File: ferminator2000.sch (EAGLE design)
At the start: 120 parts, among them CN1 MINIB, IC1 FT232RL, IC2 REF01D, Q1 STP5NA50, Q2 STP5NA50, SW1 ENCODER_SW1-PEC12, U1 DSPIC33FJ256GP510A, U2 AD8495

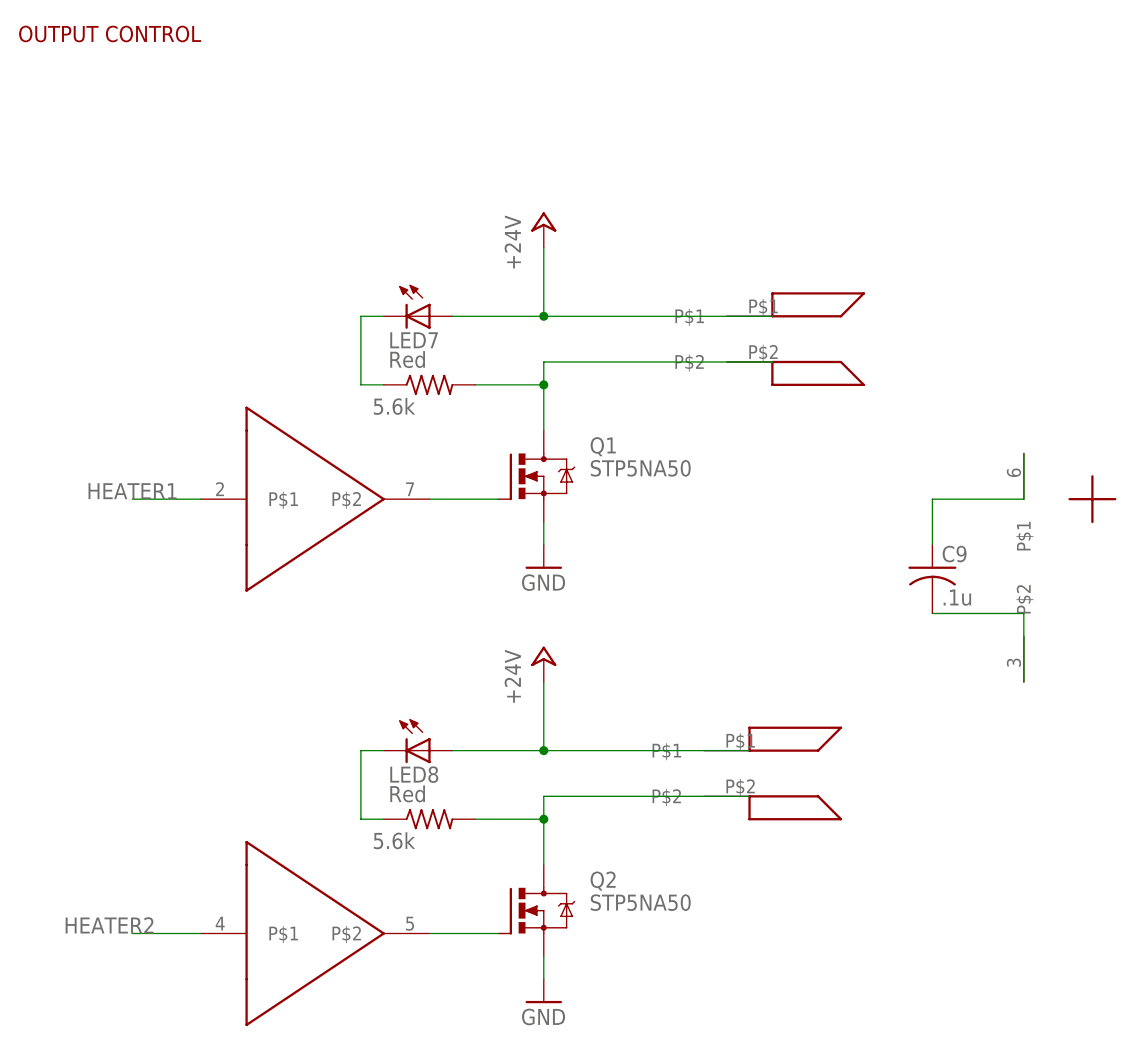
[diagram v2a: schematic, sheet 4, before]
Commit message: added power to TC4427
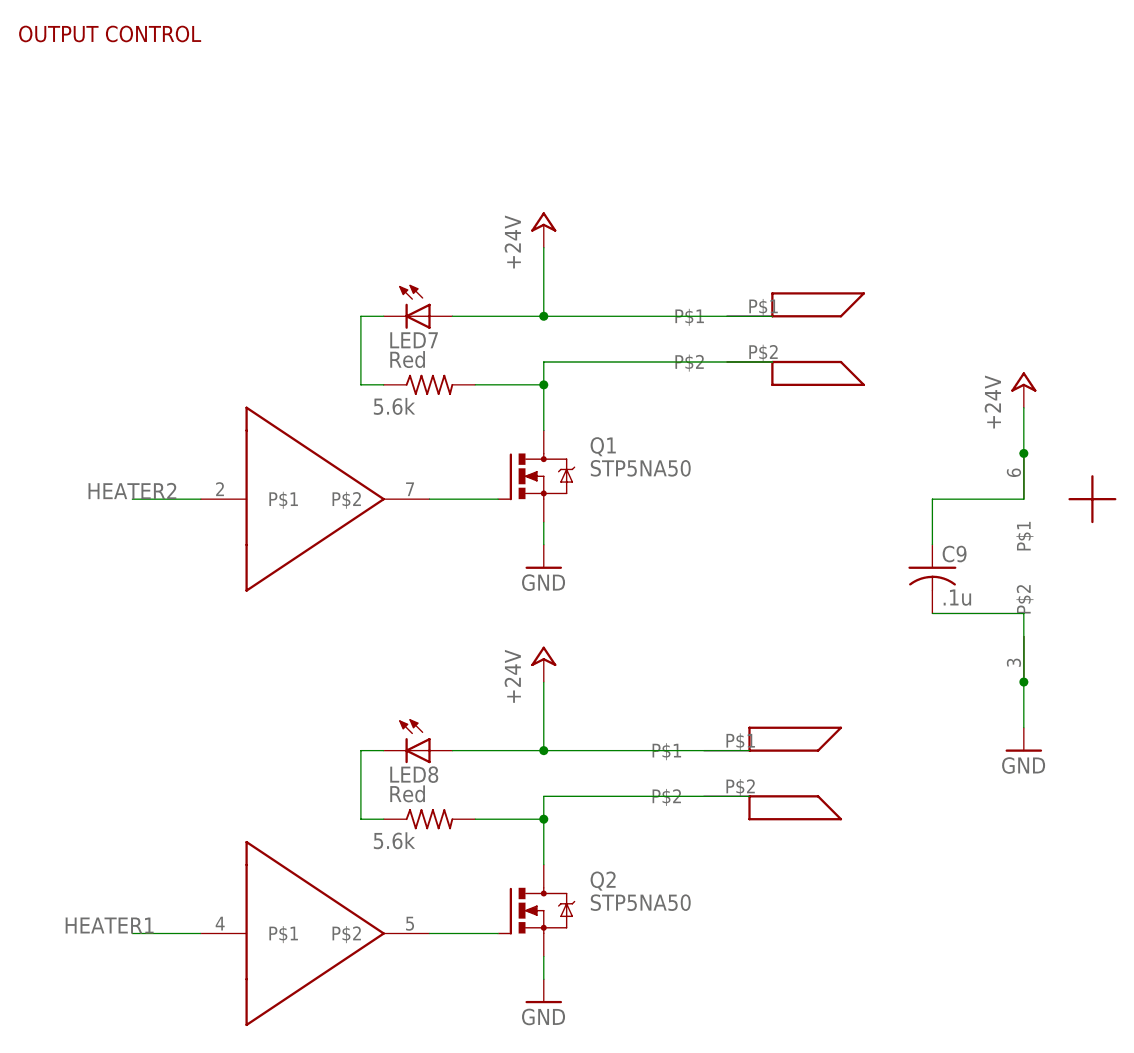
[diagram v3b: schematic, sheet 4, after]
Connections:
- removed net N$22: C9.1, U$11RAILS.P$1
- removed net N$23: C9.2, U$11RAILS.P$2
- net +24V: now also C9.1, U$11RAILS.P$1
- net GND: now also C9.2, U$11RAILS.P$2
- net HEATER1: now also U$11B.P$1, U1.AN27/RE3; no longer U$11A.P$1, U1.AN28/RE4
- net HEATER2: now also U$11A.P$1, U1.AN28/RE4; no longer U$11B.P$1, U1.AN27/RE3
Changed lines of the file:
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@@
 <part name="GND4" library="supply1" deviceset="GND" device=""/>
 <part name="VDD9" library="supply1" deviceset="VDD" device=""/>
+<part name="P+7" library="supply1" deviceset="+24V" device=""/>
+<part name="GND5" library="supply1" deviceset="GND" device=""/>
 </parts>
 <sheets>
@@
 <net name="HEATER2" class="0">
 <segment>
+<pinref part="U1" gate="G$1" pin="AN28/RE4"/>
+<wire x1="459.74" y1="177.8" x2="459.74" y2="185.42" width="0.1524" layer="91"/>
+<wire x1="459.74" y1="185.42" x2="449.58" y2="185.42" width="0.1524" layer="91"/>
+<label x="449.58" y="185.42" size="1.778" layer="95"/>
+</segment>
+</net>
+<net name="HEATER1" class="0">
+<segment>
 <pinref part="U1" gate="G$1" pin="AN27/RE3"/>
 <wire x1="459.74" y1="175.26" x2="462.28" y2="175.26" width="0.1524" layer="91"/>
@@
 <wire x1="462.28" y1="187.96" x2="449.58" y2="187.96" width="0.1524" layer="91"/>
 <label x="449.58" y="187.96" size="1.778" layer="95"/>
-</segment>
-</net>
-<net name="HEATER1" class="0">
-<segment>
-<pinref part="U1" gate="G$1" pin="AN28/RE4"/>
-<wire x1="459.74" y1="177.8" x2="459.74" y2="185.42" width="0.1524" layer="91"/>
-<wire x1="459.74" y1="185.42" x2="449.58" y2="185.42" width="0.1524" layer="91"/>
-<label x="449.58" y="185.42" size="1.778" layer="95"/>
 </segment>
 </net>
@@
 <attribute name="VALUE" x="123.19" y="55.118" size="1.778" layer="96"/>
 </instance>
+<instance part="P+7" gate="1" x="195.58" y="106.68"/>
+<instance part="GND5" gate="1" x="195.58" y="66.04"/>
 </instances>
 <busses>
@@
 <junction x="142.24" y="66.04"/>
 </segment>
-</net>
-<net name="N$20" class="0">
-<segment>
-<pinref part="U$11" gate="A" pin="P$2"/>
-<pinref part="Q1" gate="T" pin="G"/>
-<wire x1="129.54" y1="93.98" x2="137.16" y2="93.98" width="0.1524" layer="91"/>
-</segment>
-</net>
-<net name="GND" class="0">
-<segment>
-<pinref part="GND13" gate="1" pin="GND"/>
-<pinref part="Q1" gate="T" pin="S"/>
-<wire x1="142.24" y1="88.9" x2="142.24" y2="91.44" width="0.1524" layer="91"/>
-</segment>
-<segment>
-<pinref part="GND14" gate="1" pin="GND"/>
-<pinref part="Q2" gate="T" pin="S"/>
-<wire x1="142.24" y1="40.64" x2="142.24" y2="43.18" width="0.1524" layer="91"/>
-</segment>
-</net>
-<net name="N$21" class="0">
-<segment>
-<pinref part="Q2" gate="T" pin="G"/>
-<pinref part="U$11" gate="B" pin="P$2"/>
-<wire x1="137.16" y1="45.72" x2="129.54" y2="45.72" width="0.1524" layer="91"/>
-</segment>
-</net>
-<net name="HEATER1" class="0">
-<segment>
-<pinref part="U$11" gate="A" pin="P$1"/>
-<wire x1="104.14" y1="93.98" x2="96.52" y2="93.98" width="0.1524" layer="91"/>
-<label x="91.44" y="93.98" size="1.778" layer="95"/>
-</segment>
-</net>
-<net name="HEATER2" class="0">
-<segment>
-<pinref part="U$11" gate="B" pin="P$1"/>
-<wire x1="104.14" y1="45.72" x2="96.52" y2="45.72" width="0.1524" layer="91"/>
-<label x="88.9" y="45.72" size="1.778" layer="95"/>
-</segment>
-</net>
-<net name="N$22" class="0">
 <segment>
 <pinref part="C9" gate="G$1" pin="1"/>
@@
 <pinref part="U$11" gate="RAILS" pin="P$1"/>
 <wire x1="195.58" y1="93.98" x2="195.58" y2="99.06" width="0.1524" layer="91"/>
-</segment>
-</net>
-<net name="N$23" class="0">
+<pinref part="P+7" gate="1" pin="+24V"/>
+<wire x1="195.58" y1="104.14" x2="195.58" y2="99.06" width="0.1524" layer="91"/>
+<junction x="195.58" y="99.06"/>
+</segment>
+</net>
+<net name="N$20" class="0">
+<segment>
+<pinref part="U$11" gate="A" pin="P$2"/>
+<pinref part="Q1" gate="T" pin="G"/>
+<wire x1="129.54" y1="93.98" x2="137.16" y2="93.98" width="0.1524" layer="91"/>
+</segment>
+</net>
+<net name="GND" class="0">
+<segment>
+<pinref part="GND13" gate="1" pin="GND"/>
+<pinref part="Q1" gate="T" pin="S"/>
+<wire x1="142.24" y1="88.9" x2="142.24" y2="91.44" width="0.1524" layer="91"/>
+</segment>
+<segment>
+<pinref part="GND14" gate="1" pin="GND"/>
+<pinref part="Q2" gate="T" pin="S"/>
+<wire x1="142.24" y1="40.64" x2="142.24" y2="43.18" width="0.1524" layer="91"/>
+</segment>
 <segment>
 <pinref part="C9" gate="G$1" pin="2"/>
@@
 <pinref part="U$11" gate="RAILS" pin="P$2"/>
 <wire x1="195.58" y1="81.28" x2="195.58" y2="73.66" width="0.1524" layer="91"/>
+<pinref part="GND5" gate="1" pin="GND"/>
+<wire x1="195.58" y1="68.58" x2="195.58" y2="73.66" width="0.1524" layer="91"/>
+<junction x="195.58" y="73.66"/>
+</segment>
+</net>
+<net name="N$21" class="0">
+<segment>
+<pinref part="Q2" gate="T" pin="G"/>
+<pinref part="U$11" gate="B" pin="P$2"/>
+<wire x1="137.16" y1="45.72" x2="129.54" y2="45.72" width="0.1524" layer="91"/>
+</segment>
+</net>
+<net name="HEATER2" class="0">
+<segment>
+<pinref part="U$11" gate="A" pin="P$1"/>
+<wire x1="104.14" y1="93.98" x2="96.52" y2="93.98" width="0.1524" layer="91"/>
+<label x="91.44" y="93.98" size="1.778" layer="95"/>
 </segment>
 </net>
@@
 </segment>
 </net>
+<net name="HEATER1" class="0">
+<segment>
+<pinref part="U$11" gate="B" pin="P$1"/>
+<wire x1="104.14" y1="45.72" x2="96.52" y2="45.72" width="0.1524" layer="91"/>
+<label x="88.9" y="45.72" size="1.778" layer="95"/>
+</segment>
+</net>
